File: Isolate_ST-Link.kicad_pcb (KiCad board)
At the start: 2 copper layers, 50 x 50 mm, 66 parts, among them J1 USB_OTG, J2 CONN_01X06, J3 CONN_01X04, J4 CONN_01X02, J5 CONN_01X02, J6 GS2, Q1 BSS138, U1 MAU10x, U2 ADuM4160, U3 APE8865NR-33-HF-3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

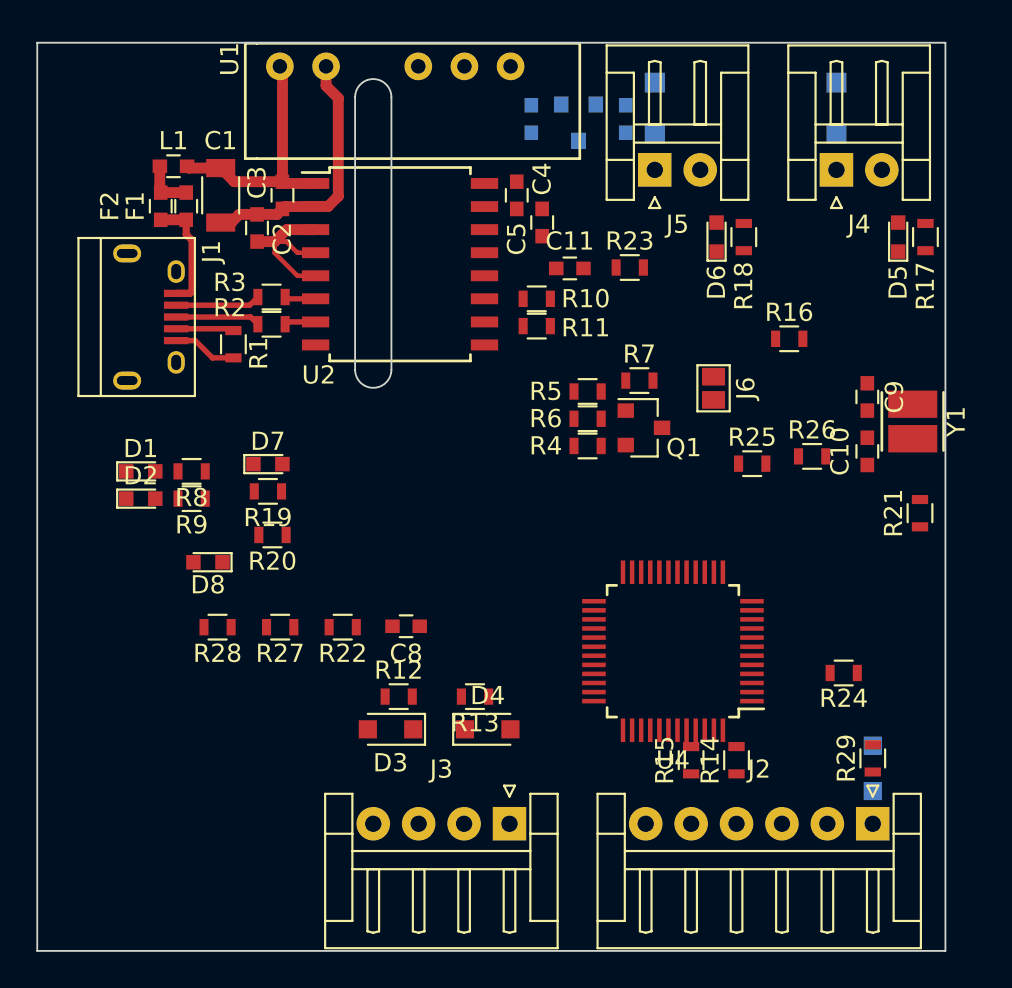
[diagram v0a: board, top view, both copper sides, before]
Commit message: 1次側のベタGND作った
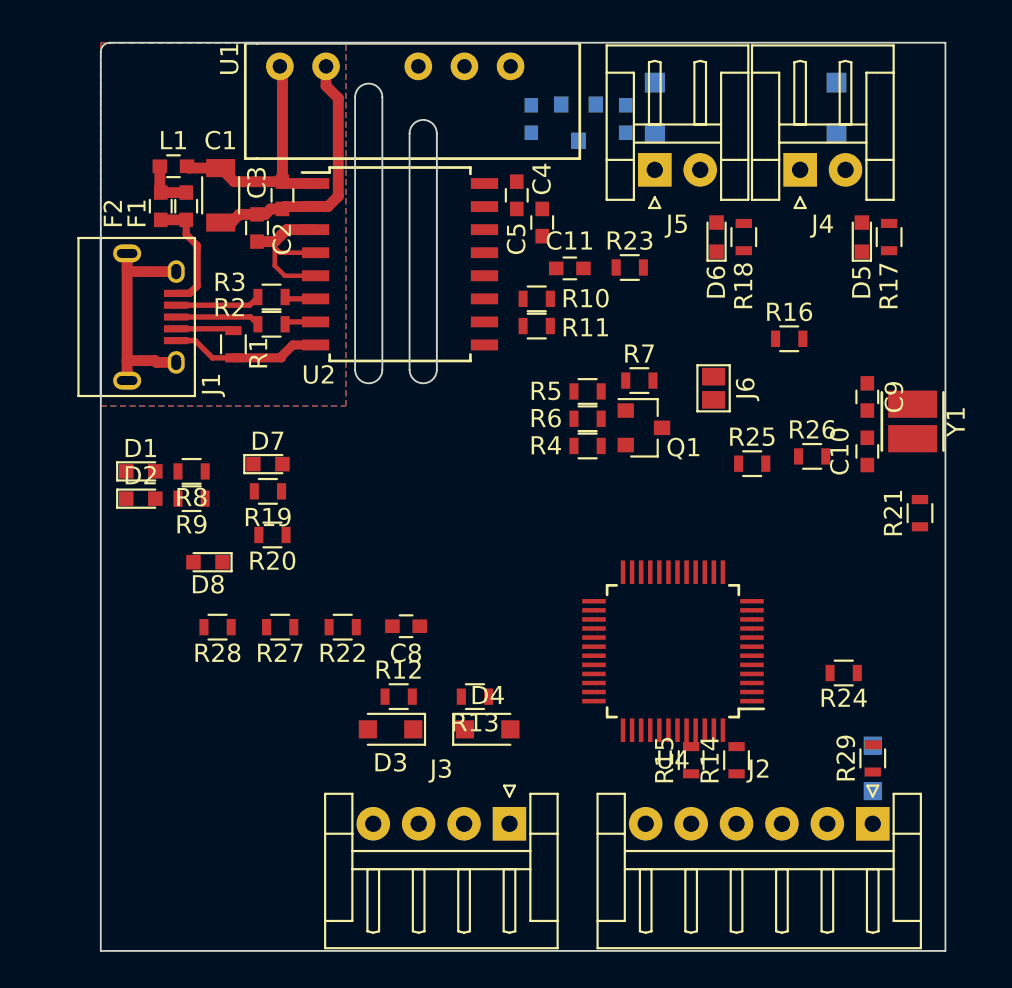
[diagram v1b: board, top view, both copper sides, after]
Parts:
- moved D5 2.00 mm to (195.4, 60.7)
- moved J4 2.00 mm to (192.0, 57.0)
- moved R17 2.00 mm to (196.9, 60.7)
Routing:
- net GNDPWR: track 18.1 -> 35.4 mm
- net Net-(C3-Pad2): track 9.40 -> 10.00 mm
- added copper zone on B.Cu, net GNDPWR
- added copper zone on F.Cu, net GNDPWR
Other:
- board size 50 x 50 mm -> 46.5 x 50 mm
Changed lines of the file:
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@@
   (general
     (links 140)
-    (no_connects 140)
-    (area 149.949999 49.949999 200.050001 100.050001)
+    (no_connects 119)
+    (area 153.449999 49.949999 200.050001 100.050001)
     (thickness 1.6)
-    (drawings 8)
-    (tracks 52)
+    (drawings 13)
+    (tracks 67)
     (zones 0)
     (modules 66)
@@
   )
   (setup
-    (last_trace_width 0.6)
+    (last_trace_width 0.4)
     (user_trace_width 0.3)
     (user_trace_width 0.4)
@@
     (user_trace_width 0.6)
     (trace_clearance 0.2)
-    (zone_clearance 0.508)
+    (zone_clearance 0.254)
     (zone_45_only no)
     (trace_min 0.2)
@@
     (pad_to_mask_clearance 0)
     (aux_axis_origin 0 0)
-    (visible_elements FFFEFF7F)
+    (visible_elements 7FFFFFFF)
     (pcbplotparams
       (layerselection 0x00030_80000001)
@@
   )
   (module LEDs:LED_0603 (layer F.Cu)
-    (at 197.4 60.7 90)
+    (at 195.4 60.7 90)
     (descr "LED 0603 smd package")
     (tags "LED led 0603 SMD smd SMT smt smdled SMDLED smtled SMTLED")
@@
     (tags "capacitor 0603")
     (attr smd)
-    (fp_text reference F1 (at 0 2.8 270) (layer F.SilkS)
+    (fp_text reference F1 (at 0.4 2.7 270) (layer F.SilkS)
       (effects (font (size 1 1) (thickness 0.15)))
     )
@@
     (tags "capacitor 0603")
     (attr smd)
-    (fp_text reference F2 (at 0 2.8 270) (layer F.SilkS)
+    (fp_text reference F2 (at 0.4 2.6 270) (layer F.SilkS)
       (effects (font (size 1 1) (thickness 0.15)))
     )
@@
     (tags "USB USB_B USB_micro USB_OTG")
     (attr smd)
-    (fp_text reference J1 (at -3.6 -3.3 450) (layer F.SilkS)
+    (fp_text reference J1 (at 3.7 -3.3 450) (layer F.SilkS)
       (effects (font (size 1 1) (thickness 0.15)))
     )
@@
   )
   (module Connectors_JST:JST_EH_S02B-EH_02x2.50mm_Angled (layer F.Cu)
-    (at 194 57)
+    (at 192 57)
     (descr "JST EH series connector, S02B-EH, 2.50mm pitch, side entry")
     (tags "connector jst eh side horizontal angled")
@@
   )
   (module Resistors_SMD:R_0603 (layer F.Cu)
-    (at 198.9 60.7 270)
+    (at 196.9 60.7 270)
     (descr "Resistor SMD 0603, reflow soldering, Vishay (see dcrcw.pdf)")
     (tags "resistor 0603")
@@
     )
   )
-  (gr_arc (start 168.5 68) (end 169.5 68) (angle 180) (layer Edge.Cuts) (width 0.1))
-  (gr_arc (start 168.5 53) (end 167.5 53) (angle 180) (layer Edge.Cuts) (width 0.1))
-  (gr_line (start 169.5 68) (end 169.5 53) (layer Edge.Cuts) (width 0.1))
+  (gr_arc (start 154 50.5) (end 153.5 50.5) (angle 90) (layer Edge.Cuts) (width 0.1))
+  (gr_arc (start 171.25 68) (end 172 68) (angle 180) (layer Edge.Cuts) (width 0.1))
+  (gr_arc (start 171.25 55) (end 170.5 55) (angle 180) (layer Edge.Cuts) (width 0.1))
+  (gr_line (start 172 68) (end 172 55) (layer Edge.Cuts) (width 0.1))
+  (gr_line (start 170.5 55) (end 170.5 68) (layer Edge.Cuts) (width 0.1))
+  (gr_arc (start 168.25 68) (end 169 68) (angle 180) (layer Edge.Cuts) (width 0.1))
+  (gr_arc (start 168.25 53) (end 167.5 53) (angle 180) (layer Edge.Cuts) (width 0.1))
+  (gr_line (start 169 68) (end 169 53) (layer Edge.Cuts) (width 0.1))
   (gr_line (start 167.5 53) (end 167.5 68) (layer Edge.Cuts) (width 0.1))
   (gr_line (start 200 100) (end 200 50) (layer Edge.Cuts) (width 0.1))
-  (gr_line (start 150 100) (end 200 100) (layer Edge.Cuts) (width 0.1))
-  (gr_line (start 150 50) (end 150 100) (layer Edge.Cuts) (width 0.1))
-  (gr_line (start 200 50) (end 150 50) (layer Edge.Cuts) (width 0.1))
+  (gr_line (start 153.5 100) (end 200 100) (layer Edge.Cuts) (width 0.1))
+  (gr_line (start 153.5 50.5) (end 153.5 100) (layer Edge.Cuts) (width 0.1))
+  (gr_line (start 200 50) (end 154 50) (layer Edge.Cuts) (width 0.1))
   (segment (start 163.5 57.65) (end 163.5 51.44) (width 0.6) (layer F.Cu) (net 1))
   (segment (start 163.5 51.44) (end 163.36 51.3) (width 0.6) (layer F.Cu) (net 1))
@@
   (segment (start 165.325001 57.75) (end 163.6 57.75) (width 0.6) (layer F.Cu) (net 1))
   (segment (start 163.6 57.75) (end 163.5 57.65) (width 0.6) (layer F.Cu) (net 1))
+  (segment (start 163.45 67.35) (end 163.45 67.265001) (width 0.5) (layer F.Cu) (net 2))
+  (segment (start 163.45 67.265001) (end 164.075001 66.64) (width 0.5) (layer F.Cu) (net 2))
+  (segment (start 164.075001 66.64) (end 165.325001 66.64) (width 0.5) (layer F.Cu) (net 2))
+  (segment (start 160.8 67.35) (end 163.45 67.35) (width 0.5) (layer F.Cu) (net 2))
+  (segment (start 154.95 68.6) (end 154.95 67.5) (width 0.6) (layer F.Cu) (net 2))
+  (segment (start 154.95 67.5) (end 154.95 62.5) (width 0.6) (layer F.Cu) (net 2))
+  (segment (start 157.65 67.6) (end 156.575 67.6) (width 0.6) (layer F.Cu) (net 2))
+  (segment (start 156.575 67.6) (end 156.475 67.5) (width 0.6) (layer F.Cu) (net 2))
+  (segment (start 156.475 67.5) (end 154.95 67.5) (width 0.6) (layer F.Cu) (net 2))
+  (segment (start 154.95 62.5) (end 154.95 61.6) (width 0.6) (layer F.Cu) (net 2))
+  (segment (start 157.65 62.6) (end 155.05 62.6) (width 0.6) (layer F.Cu) (net 2))
+  (segment (start 155.05 62.6) (end 154.95 62.5) (width 0.6) (layer F.Cu) (net 2))
+  (segment (start 162.85 59.15) (end 162.55 59.45) (width 0.6) (layer F.Cu) (net 2))
+  (segment (start 162.55 59.45) (end 162.1 59.45) (width 0.6) (layer F.Cu) (net 2))
+  (segment (start 163.5 59.15) (end 162.85 59.15) (width 0.6) (layer F.Cu) (net 2))
   (segment (start 165.9 51.3) (end 165.9 52.37763) (width 0.6) (layer F.Cu) (net 2))
   (segment (start 165.9 52.37763) (end 166.575002 53.052632) (width 0.6) (layer F.Cu) (net 2))
@@
   (segment (start 161.125 59.45) (end 162.1 59.45) (width 0.6) (layer F.Cu) (net 2))
   (segment (start 160.1 59.9) (end 160.7 59.9) (width 0.6) (layer F.Cu) (net 2))
-  (segment (start 162.1 59.45) (end 163.2 59.45) (width 0.6) (layer F.Cu) (net 2))
-  (segment (start 163.2 59.45) (end 163.5 59.15) (width 0.6) (layer F.Cu) (net 2))
   (segment (start 165.325001 59.02) (end 163.63 59.02) (width 0.6) (layer F.Cu) (net 2))
   (segment (start 163.63 59.02) (end 163.5 59.15) (width 0.6) (layer F.Cu) (net 2))
-  (segment (start 163.075 61.579999) (end 163.075 60.95) (width 0.25) (layer F.Cu) (net 3))
-  (segment (start 165.325001 62.83) (end 164.325001 62.83) (width 0.25) (layer F.Cu) (net 3))
-  (segment (start 164.325001 62.83) (end 163.075 61.579999) (width 0.25) (layer F.Cu) (net 3))
-  (segment (start 165.325001 61.56) (end 164.325001 61.56) (width 0.25) (layer F.Cu) (net 3))
-  (segment (start 164.325001 61.56) (end 163.715001 60.95) (width 0.25) (layer F.Cu) (net 3))
-  (segment (start 163.715001 60.95) (end 163.075 60.95) (width 0.25) (layer F.Cu) (net 3))
+  (segment (start 163.075 61.275) (end 163.36 61.56) (width 0.25) (layer F.Cu) (net 3))
+  (segment (start 163.36 61.56) (end 165.325001 61.56) (width 0.25) (layer F.Cu) (net 3))
+  (segment (start 163.075 60.95) (end 163.075 61.275) (width 0.25) (layer F.Cu) (net 3))
+  (segment (start 163.075 62.275) (end 163.63 62.83) (width 0.25) (layer F.Cu) (net 3))
+  (segment (start 163.63 62.83) (end 165.325001 62.83) (width 0.25) (layer F.Cu) (net 3))
+  (segment (start 163.075 60.95) (end 163.075 62.275) (width 0.25) (layer F.Cu) (net 3))
   (segment (start 162.1 60.95) (end 163.075 60.95) (width 0.6) (layer F.Cu) (net 3))
   (segment (start 163.075 60.95) (end 163.735 60.29) (width 0.6) (layer F.Cu) (net 3))
@@
   (segment (start 156.75 56.8) (end 156.75 58.2) (width 0.6) (layer F.Cu) (net 24))
   (segment (start 156.75 58.2) (end 156.8 58.25) (width 0.6) (layer F.Cu) (net 24))
+  (segment (start 158.8 63.4) (end 158.8 61.3) (width 0.4) (layer F.Cu) (net 25))
+  (segment (start 158.2 60.55) (end 158.8 61.15) (width 0.4) (layer F.Cu) (net 25))
+  (segment (start 158.2 59.75) (end 158.2 60.55) (width 0.4) (layer F.Cu) (net 25))
+  (segment (start 158.8 61.15) (end 158.8 61.3) (width 0.4) (layer F.Cu) (net 25))
+  (segment (start 158.4 63.8) (end 158.8 63.4) (width 0.4) (layer F.Cu) (net 25))
   (segment (start 156.8 59.75) (end 158.2 59.75) (width 0.6) (layer F.Cu) (net 25))
   (segment (start 158.4 63.8) (end 158.52501 63.67499) (width 0.4) (layer F.Cu) (net 25))
-  (segment (start 158.52501 63.67499) (end 158.52501 60.87501) (width 0.4) (layer F.Cu) (net 25))
-  (segment (start 158.52501 60.87501) (end 158.2 60.55) (width 0.4) (layer F.Cu) (net 25))
-  (segment (start 158.2 60.55) (end 158.2 59.75) (width 0.4) (layer F.Cu) (net 25))
   (segment (start 157.65 63.8) (end 158.4 63.8) (width 0.4) (layer F.Cu) (net 25))
   (segment (start 157.65 64.45) (end 161.7 64.45) (width 0.3) (layer F.Cu) (net 26))
@@
   (segment (start 165.325001 64.1) (end 163.75 64.1) (width 0.3) (layer F.Cu) (net 37))
   (segment (start 163.75 64.1) (end 163.65 64) (width 0.3) (layer F.Cu) (net 37))
+  (zone (net 2) (net_name GNDPWR) (layer F.Cu) (hatch edge 0.508)
+    (connect_pads (clearance 0.254))
+    (min_thickness 0.254)
+    (fill yes (arc_segments 16) (thermal_gap 0.508) (thermal_bridge_width 0.508))
+    (polygon
+      (pts
+        (xy 153.5 70) (xy 167 70) (xy 167 50) (xy 153.5 50)
+      )
+    )
+  )
+  (zone (net 2) (net_name GNDPWR) (layer B.Cu) (hatch edge 0.508)
+    (connect_pads (clearance 0.254))
+    (min_thickness 0.254)
+    (fill yes (arc_segments 16) (thermal_gap 0.508) (thermal_bridge_width 0.508))
+    (polygon
+      (pts
+        (xy 153.5 70) (xy 167 70) (xy 167 50) (xy 153.5 50)
+      )
+    )
+  )
 )

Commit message: AW進捗
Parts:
- C11, C8, J6, R17, R18, R19, R20, R21, R22, R23, R24, R25, R26, R27, R28, R29: moved to B.Cu
- D3, D4: footprint Diodes_SMD:D_SOD-323_HandSoldering -> Diodes_SMD:D_SOD-323
- moved R16 32.0 mm to (160.9, 76.1), turned to 90 degrees
- moved J2 29.6 mm to (168.8, 81.2)
- moved C9 28.6 mm to (173.1, 87.0), turned to 90 degrees
- moved R14 28.0 mm to (163.9, 76.1)
- moved D8 27.7 mm to (186.0, 86.5)
- moved R24 27.6 mm to (169.1, 73.8), turned to 90 degrees
- moved Y1 27.6 mm to (173.8, 83.7), turned to 0 degrees
- moved R15 27.1 mm to (162.4, 76.1)
- moved R19 26.8 mm to (187.4, 85.0)
- moved R20 26.2 mm to (187.4, 86.5)
- moved D7 26.2 mm to (186.0, 85.1), turned to 180 degrees
- moved C10 25.7 mm to (174.5, 87.0)
- moved R21 24.1 mm to (174.8, 79.5), turned to 180 degrees
- moved J3 21.6 mm to (185.8, 73.7), turned to 270 degrees
- moved R28 19.4 mm to (179.3, 83.1), turned to 90 degrees
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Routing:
- net GND: track 0.00 -> 79.1 mm, vias 0 -> 6
- net +3V3: track 0.00 -> 44.7 mm, vias 0 -> 1
- net +5V: track 0.00 -> 25.6 mm, vias 0 -> 1
- net /MCU/UART_TX: track 0.00 -> 15.6 mm
- net /MCU/UART_RX: track 0.00 -> 10.7 mm
- net Net-(Q1-Pad1): track 0.00 -> 9.39 mm
- net Net-(C4-Pad2): track 0.00 -> 8.59 mm
- net Net-(R11-Pad2): track 0.00 -> 7.20 mm
- net /MCU/USB_DM: track 0.00 -> 7.18 mm
- net /MCU/USB_DP: track 0.00 -> 6.44 mm
- net GNDPWR: track 35.4 -> 40.4 mm, vias 0 -> 4
- net Net-(D9-Pad1): track 0.00 -> 2.45 mm
- net Net-(R10-Pad1): track 0.00 -> 1.67 mm
- net Net-(Q1-Pad2): track 0.00 -> 1.66 mm
- net Net-(D7-Pad1): track 0.00 -> 1.37 mm, vias 0 -> 1
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- added copper zone on B.Cu, net GND
- added copper zone on F.Cu, net GND
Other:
- board size 46.5 x 50 mm -> 39.5 x 39 mm
- board text added: "3.3V"
- board text added: "5V"
- board text added: "RX"
- board text added: "TX"
- board text added: "UART"

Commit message: 完成したのでしばらく寝かせる
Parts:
- D11: footprint Diodes_SMD:D_SOD-323_HandSoldering -> Diodes_SMD:D_SOD-323
- R14, R15, R16: moved to B.Cu
- moved D11 7.92 mm to (171.8, 87.9), turned to 180 degrees
- moved R28 6.44 mm to (174.8, 87.7), turned to 0 degrees
- moved R29 5.61 mm to (172.2, 86.1), turned to 0 degrees
- moved R16 5.19 mm to (156.9, 79.4), turned to 0 degrees
- moved R25 4.84 mm to (171.1, 81.0), turned to 180 degrees
- moved C10 4.74 mm to (177.8, 83.6)
- moved R15 4.39 mm to (159.5, 79.4), turned to 0 degrees
- moved R27 4.24 mm to (174.8, 86.1), turned to 180 degrees
- moved R14 3.76 mm to (162.1, 79.4), turned to 0 degrees
- moved C9 3.42 mm to (172.7, 83.6)
- moved R23 2.85 mm to (171.8, 79.0)
- moved J6 2.17 mm to (169.3, 72.7)
- moved R24 2.07 mm to (170.8, 74.9), turned to 0 degrees
- moved C11 1.55 mm to (172.0, 71.5)
- moved Y1 1.40 mm to (175.2, 83.6)
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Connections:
- D3 pad 1: /MCU/UART_RX -> /MCU/UART_TX
- D4 pad 1: /MCU/UART_TX -> /MCU/UART_RX
- J3 pad 2: /MCU/UART_TX -> /MCU/UART_RX
- J3 pad 3: /MCU/UART_RX -> /MCU/UART_TX
- R12 pad 2: /MCU/UART_RX -> /MCU/UART_TX
- R13 pad 2: /MCU/UART_TX -> /MCU/UART_RX
- R19 pad 1: /MCU/UART_RX -> /MCU/UART_TX
- R20 pad 1: /MCU/UART_TX -> /MCU/UART_RX
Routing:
- net GND: track 79.1 -> 185.7 mm, vias 6 -> 11
- net +3V3: track 44.7 -> 121.6 mm, vias 1 -> 4
- net T_SWO: track 0.00 -> 23.4 mm, vias 0 -> 1
- net T_JTMS: track 0.00 -> 23.2 mm, vias 0 -> 1
- net T_NRST: track 0.00 -> 21.4 mm, vias 0 -> 1
- net T_JTCK: track 0.00 -> 21.3 mm, vias 0 -> 2
- net /MCU/LED_STLINK: track 0.00 -> 19.2 mm, vias 0 -> 2
- net Net-(R27-Pad1): track 0.00 -> 15.8 mm, vias 0 -> 1
- net /MCU/USB_RENUMn: track 0.00 -> 15.1 mm, vias 0 -> 2
- net /MCU/UART_RX: track 10.7 -> 20.6 mm
- net Net-(C10-Pad2): track 0.00 -> 9.27 mm
- net Net-(C9-Pad2): track 0.00 -> 9.13 mm
- net /MCU/Vtarget: track 0.00 -> 8.70 mm, vias 0 -> 1
- net /MCU/USB_DM: track 7.18 -> 12.2 mm
- net /MCU/USB_DP: track 6.44 -> 11.5 mm
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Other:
- rule trace_min: 0.2 -> 0.1999
- board text added: "3V3"
- board text added: "GND"
- board text added: "SWD"
- board text added: "Vtgt"

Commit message: 微調整
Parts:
- moved C11 3.02 mm to (174.3, 73.5), turned to 180 degrees
- moved R24 1.31 mm to (171.2, 73.7), turned to 90 degrees
- moved D11 1.10 mm to (171.8, 86.8)
- moved R28 1.10 mm to (174.8, 86.6)
- moved R27 1.10 mm to (174.8, 85.0)
- moved R29 1.10 mm to (172.2, 85.0)
- moved R22 0.83 mm to (176.1, 70.0)
- moved R26 0.35 mm to (174.1, 71.5)
- moved J6 0.11 mm to (169.2, 72.7)
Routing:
- net GNDPWR: track 40.4 -> 156.0 mm, vias 4 -> 58
- net GND: track 185.7 -> 275.5 mm, vias 11 -> 52
- net +3V3: track 121.6 -> 150.2 mm
- net /MCU/USB_RENUMn: track 15.1 -> 17.2 mm
- net Net-(R27-Pad1): track 15.8 -> 14.6 mm
- net T_NRST: track 21.4 -> 20.6 mm
- net +5V: track 25.6 -> 24.8 mm
- net Net-(R22-Pad2): track 2.30 -> 1.71 mm
- net Net-(C11-Pad1): track 1.70 -> 2.22 mm
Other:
- board size 39.5 x 39 mm -> 39.5 x 38 mm
